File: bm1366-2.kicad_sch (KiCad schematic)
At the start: 55 parts, among them U14 BM1366_mode0, U5 MCP1824T-1202E, U6 MCP1824T-0802E

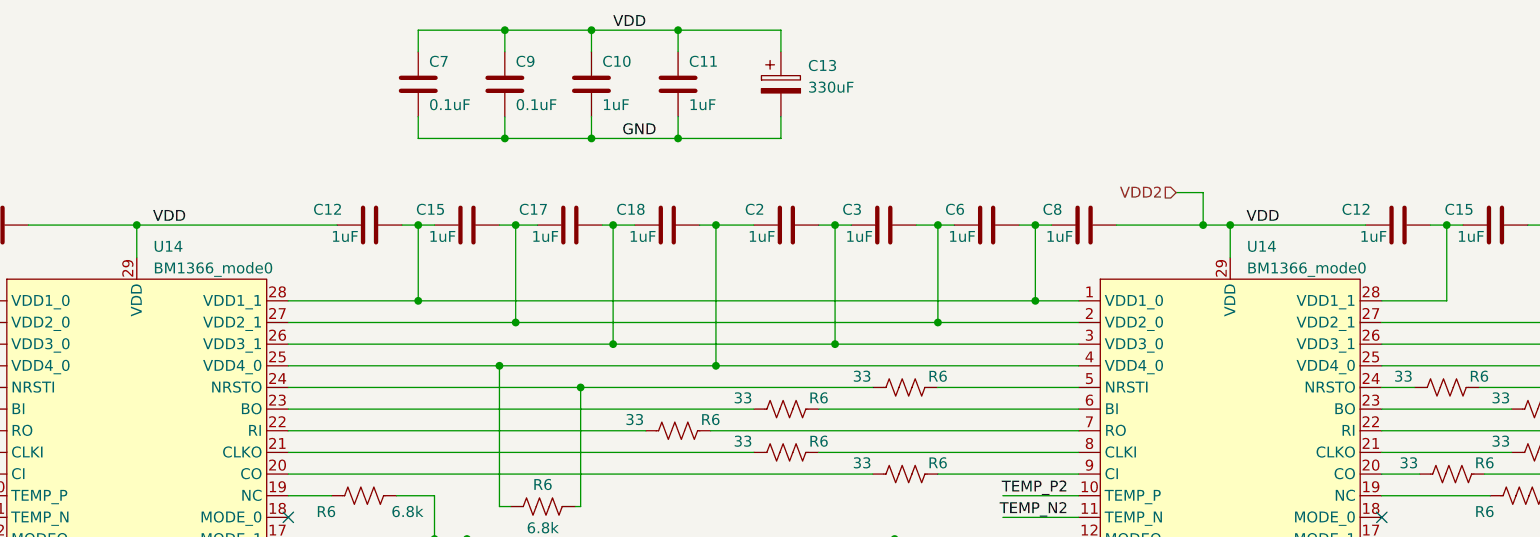
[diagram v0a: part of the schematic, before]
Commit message: cleanup parts and symbol libraries. added TMP1075
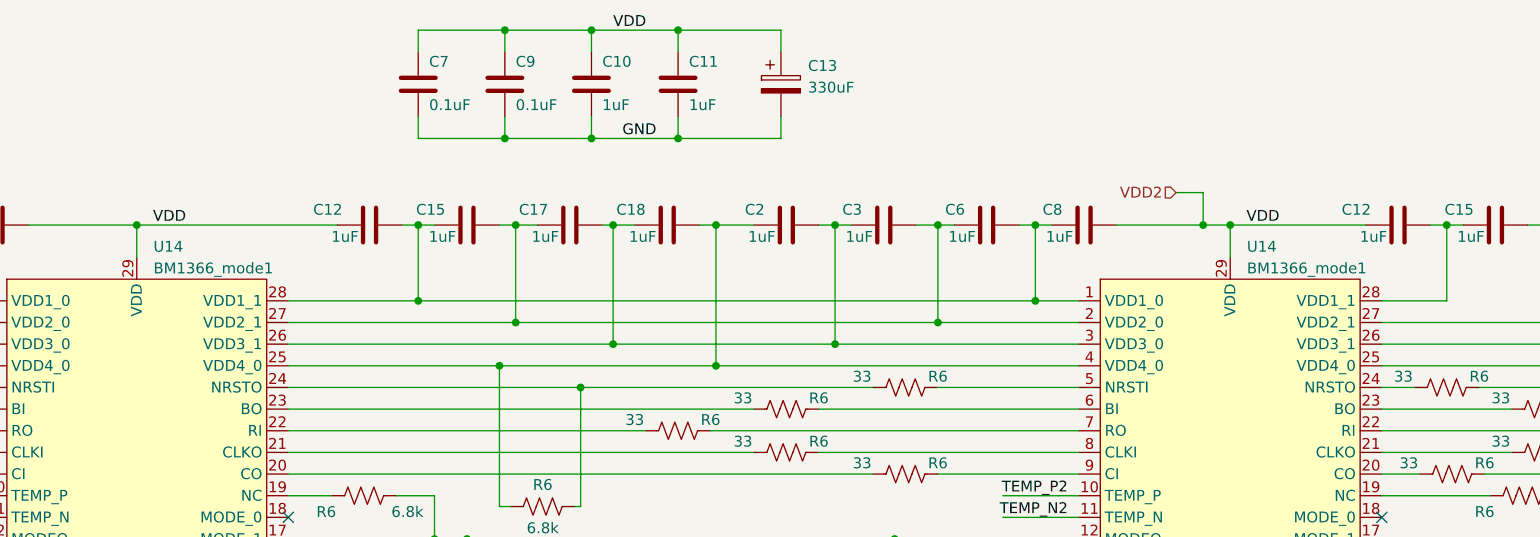
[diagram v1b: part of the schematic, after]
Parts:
- U14: value BM1366_mode0 -> BM1366_mode1; symbol Bitaxe:BM1366_mode1 -> bitaxe:BM1366_mode1
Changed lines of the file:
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@@
     )
   )
-  (symbol (lib_id "Bitaxe:BM1366_mode1") (at 201.93 86.995 0) (unit 1)
+  (symbol (lib_id "bitaxe:BM1366_mode1") (at 201.93 86.995 0) (unit 1)
     (in_bom yes) (on_board yes) (dnp no) (fields_autoplaced)
     (property "Reference" "U14" (at 203.8859 62.865 0)
       (effects (font (size 1.27 1.27)) (justify left))
     )
-    (property "Value" "BM1366_mode0" (at 203.8859 65.405 0)
+    (property "Value" "BM1366_mode1" (at 203.8859 65.405 0)
       (effects (font (size 1.27 1.27)) (justify left))
     )
@@
     )
   )
-  (symbol (lib_id "Bitaxe:BM1366_mode1") (at 73.66 86.995 0) (unit 1)
+  (symbol (lib_id "bitaxe:BM1366_mode1") (at 73.66 86.995 0) (unit 1)
     (in_bom yes) (on_board yes) (dnp no) (fields_autoplaced)
     (property "Reference" "U14" (at 75.6159 62.865 0)
       (effects (font (size 1.27 1.27)) (justify left))
     )
-    (property "Value" "BM1366_mode0" (at 75.6159 65.405 0)
+    (property "Value" "BM1366_mode1" (at 75.6159 65.405 0)
       (effects (font (size 1.27 1.27)) (justify left))
     )

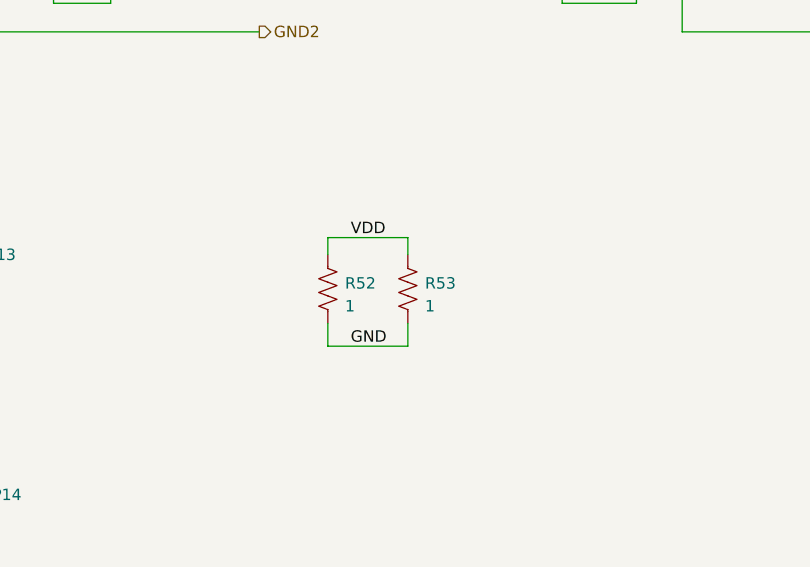
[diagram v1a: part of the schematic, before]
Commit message: added EMC2302
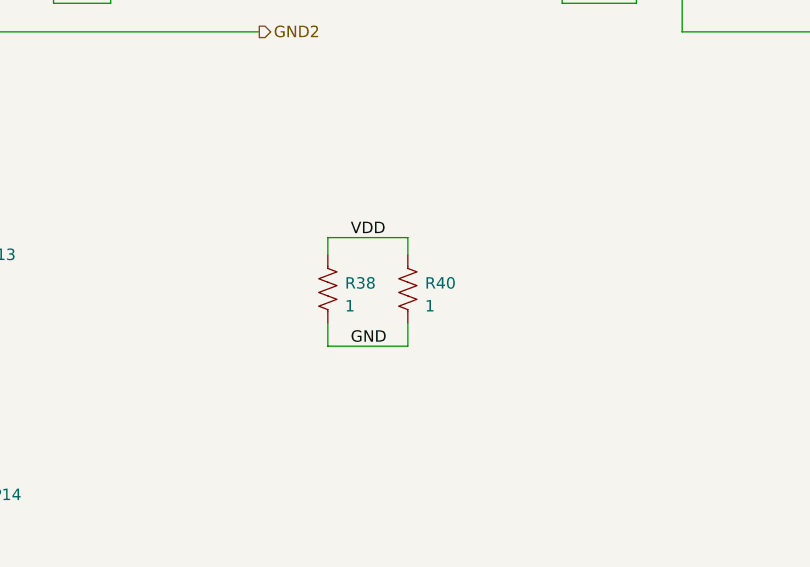
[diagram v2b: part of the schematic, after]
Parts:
- renumbered R52 to R38, R53 to R40

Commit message: moved all custom symbols and footprints to the bitaxe library
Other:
- title: (none) -> bitaxeUltraHex
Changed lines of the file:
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@@
 (kicad_sch (version 20230121) (generator eeschema)
   (paper "A")
+  (title_block
+    (title "bitaxeUltraHex")
+    (date "2023-06-11")
+    (rev "1")
+  )
   (junction (at 137.16 50.165) (diameter 0) (color 0 0 0 0)
   )

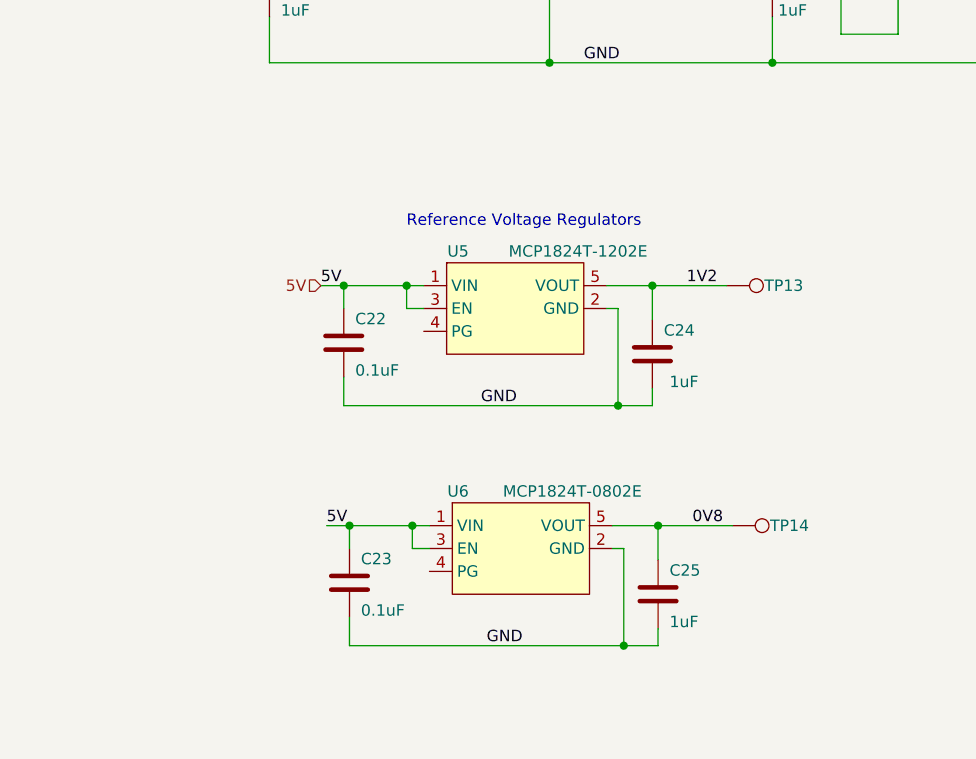
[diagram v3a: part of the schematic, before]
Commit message: Replace reference voltage regulators with new one
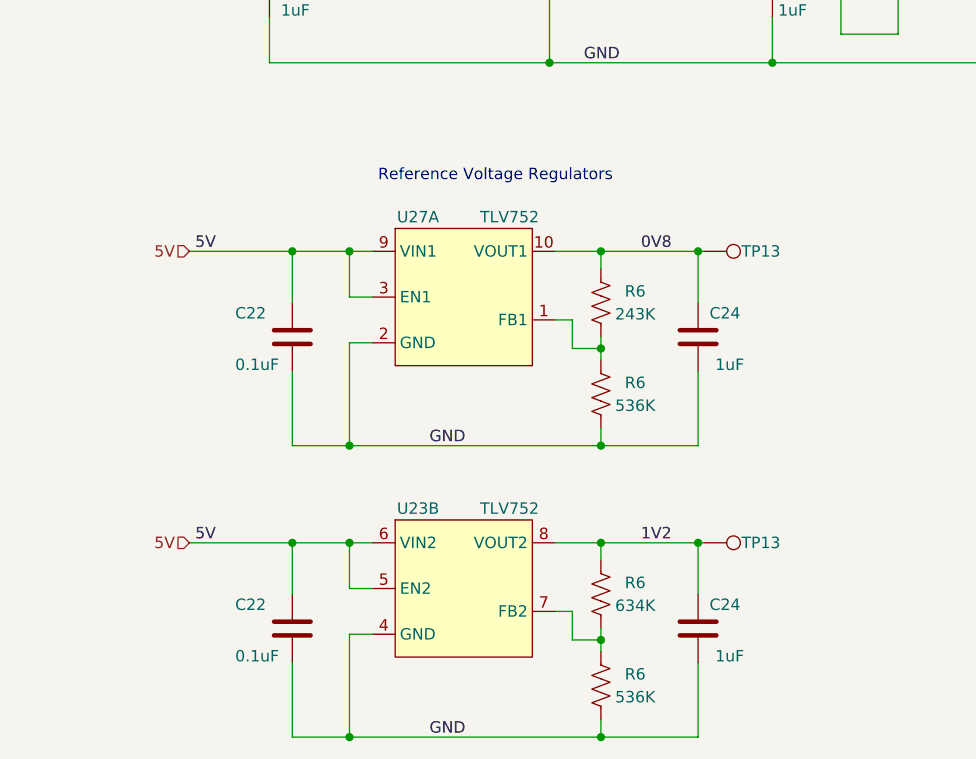
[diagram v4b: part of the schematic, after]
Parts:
- removed C22, C23: 0.1uF, Capacitor_SMD:C_0402_1005Metric, symbol Device:C
- removed C24, C25: 1uF, Capacitor_SMD:C_0402_1005Metric, symbol Device:C
- removed TP13, TP14: TestPoint, TestPoint:TestPoint_Pad_D1.5mm, symbol Connector:TestPoint
- removed U5: MCP1824T-1202E, Package_TO_SOT_SMD:SOT-23-5, symbol bitaxe:MCP1824
- removed U6: MCP1824T-0802E, Package_TO_SOT_SMD:SOT-23-5, symbol bitaxe:MCP1824
- added C22 (x2): 0.1uF, Capacitor_SMD:C_0402_1005Metric, symbol Device:C
- added C24 (x2): 1uF, Capacitor_SMD:C_0402_1005Metric, symbol Device:C
- added R6: 634K, Resistor_SMD:R_0402_1005Metric, symbol Device:R_US
- added R6 (x2): 536K, Resistor_SMD:R_0402_1005Metric, symbol Device:R_US
- added R6: 243K, Resistor_SMD:R_0402_1005Metric, symbol Device:R_US
- added TP13 (x2): TestPoint, TestPoint:TestPoint_Pad_D1.5mm, symbol Connector:TestPoint
- added U23, U27: TLV752, Package_SON:WSON-10-1EP_2.5x2.5mm_P0.5mm_EP1.2x2mm, symbol bitaxe:TLV752
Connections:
- net 0V8: now also C24.1, R6.2, TP13.1, U27.10 (VOUT1)
- net 1V2: now also C24.1, R6.2, TP13.1, U23.8 (VOUT2)
- net 5V: now also C22.1, C22.1, U23.5 (EN2), U23.6 (VIN2), U27.3 (EN1), U27.9 (VIN1)
- net GND2: now also C22.2, C22.2, C24.2, C24.2, R6.1, R6.1, U23.4 (GND), U27.2 (GND)
- new net: R6.1, R6.2, U23.7 (FB2)
- new net: R6.1, R6.2, U27.1 (FB1)

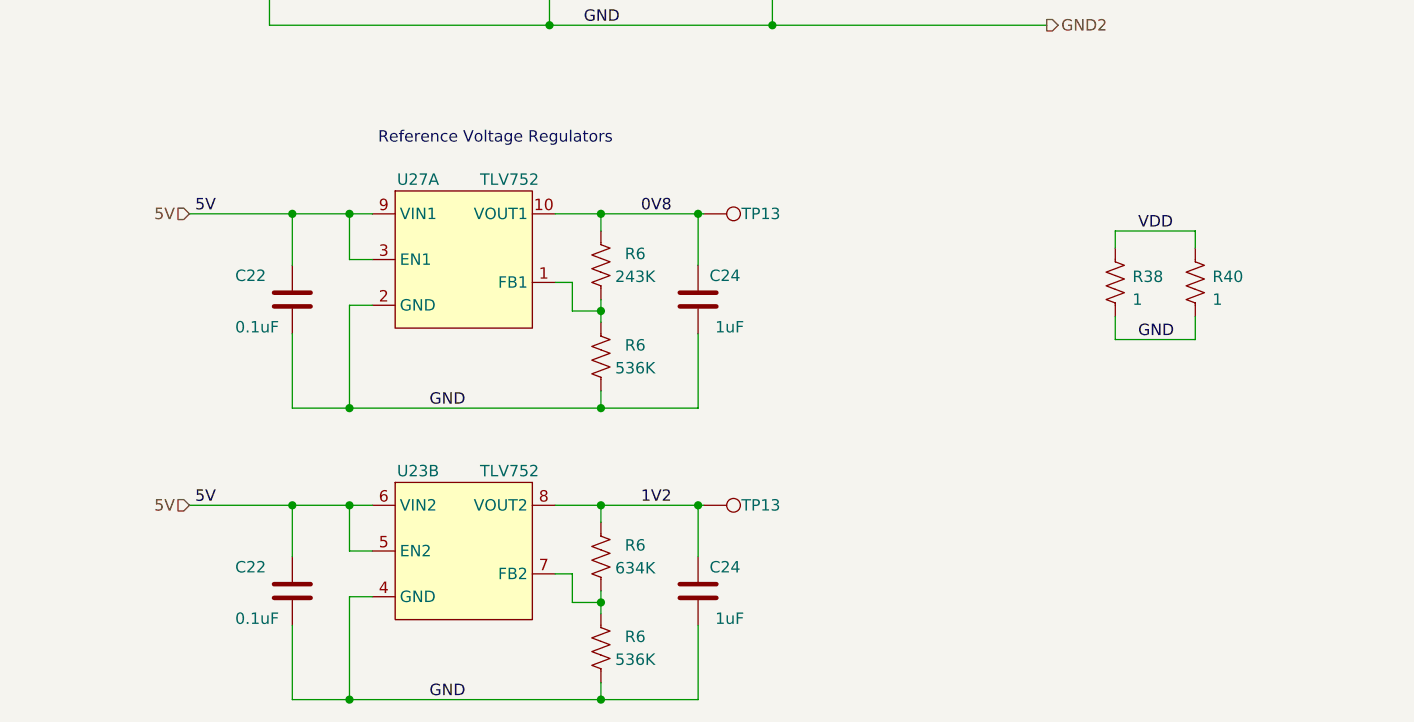
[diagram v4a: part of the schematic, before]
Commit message: switch voltage reference regulators to ADP170, reannotate
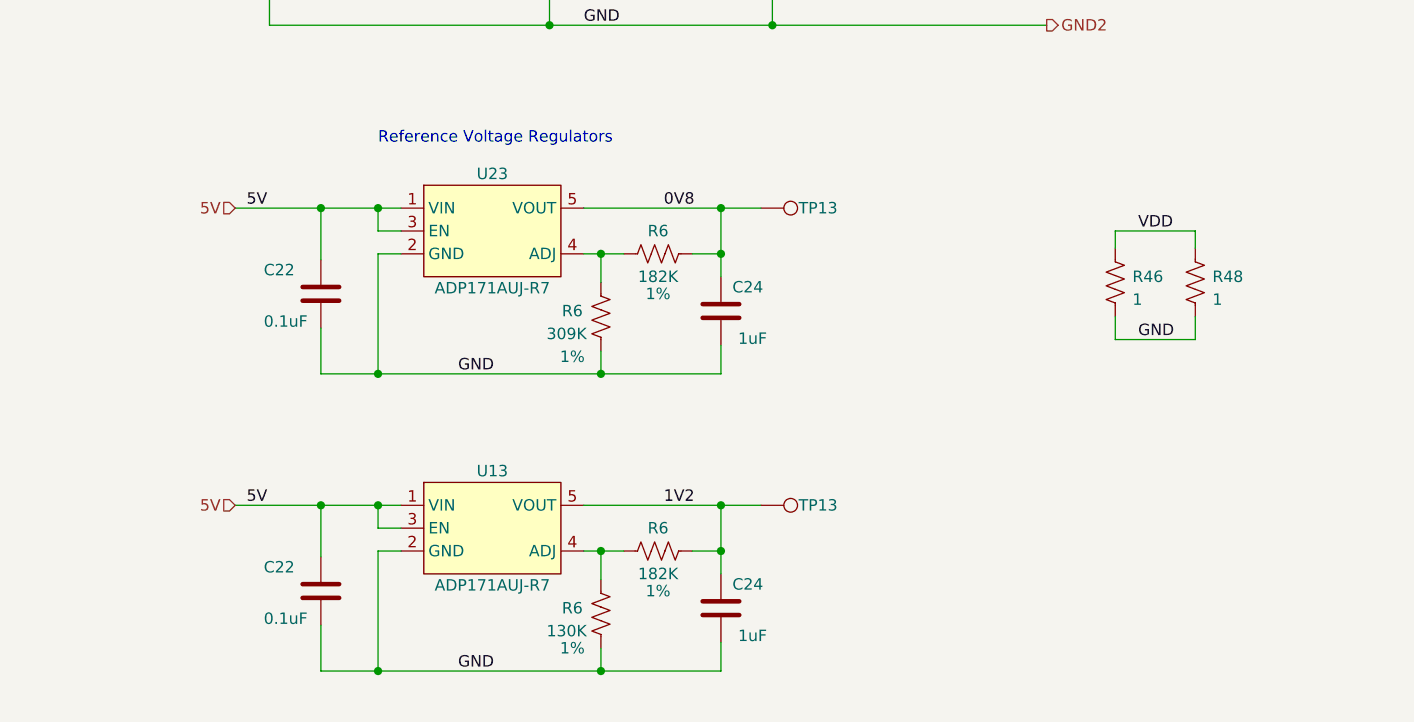
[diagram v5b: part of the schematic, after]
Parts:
- removed C22 (x2): 0.1uF, Capacitor_SMD:C_0402_1005Metric, symbol Device:C
- removed C24 (x2): 1uF, Capacitor_SMD:C_0402_1005Metric, symbol Device:C
- removed R6: 634K, Resistor_SMD:R_0402_1005Metric, symbol Device:R_US
- removed R6 (x2): 536K, Resistor_SMD:R_0402_1005Metric, symbol Device:R_US
- removed R6: 243K, Resistor_SMD:R_0402_1005Metric, symbol Device:R_US
- removed TP13 (x2): TestPoint, TestPoint:TestPoint_Pad_D1.5mm, symbol Connector:TestPoint
- removed U23, U27: TLV752, Package_SON:WSON-10-1EP_2.5x2.5mm_P0.5mm_EP1.2x2mm, symbol bitaxe:TLV752
- added C22 (x2): 0.1uF, Capacitor_SMD:C_0402_1005Metric, symbol Device:C
- added C24 (x2): 1uF, Capacitor_SMD:C_0402_1005Metric, symbol Device:C
- added R6 (x2): 182K, Resistor_SMD:R_0402_1005Metric, symbol Device:R_US
- added R6: 130K, Resistor_SMD:R_0402_1005Metric, symbol Device:R_US
- added R6: 309K, Resistor_SMD:R_0402_1005Metric, symbol Device:R_US
- added TP13 (x2): TestPoint, TestPoint:TestPoint_Pad_D1.5mm, symbol Connector:TestPoint
- added U13, U23: ADP171AUJ-R7, Package_TO_SOT_SMD:TSOT-23-5, symbol bitaxe:ADP171AUJ-R7
- renumbered R38 to R46, R40 to R48
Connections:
- net 0V8: now also C24.1, R6.1, TP13.1, U23.5 (VOUT)
- net 1V2: now also C24.1, R6.1, TP13.1, U13.5 (VOUT)
- net 5V: now also C22.1, C22.1, U13.1 (VIN), U13.3 (EN), U23.1 (VIN), U23.3 (EN)
- net GND2: now also C22.2, C22.2, C24.2, C24.2, R6.1, R6.1, U13.2 (GND), U23.2 (GND)
- new net: R6.2, R6.2, U13.4 (ADJ)
- new net: R6.2, R6.2, U23.4 (ADJ)
